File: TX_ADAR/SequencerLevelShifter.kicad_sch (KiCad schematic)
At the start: 12 parts, among them U15 TXB0101DBV, U16 TXB0101DBV, U17 TXB0101DBV, U18 TXB0101DBV

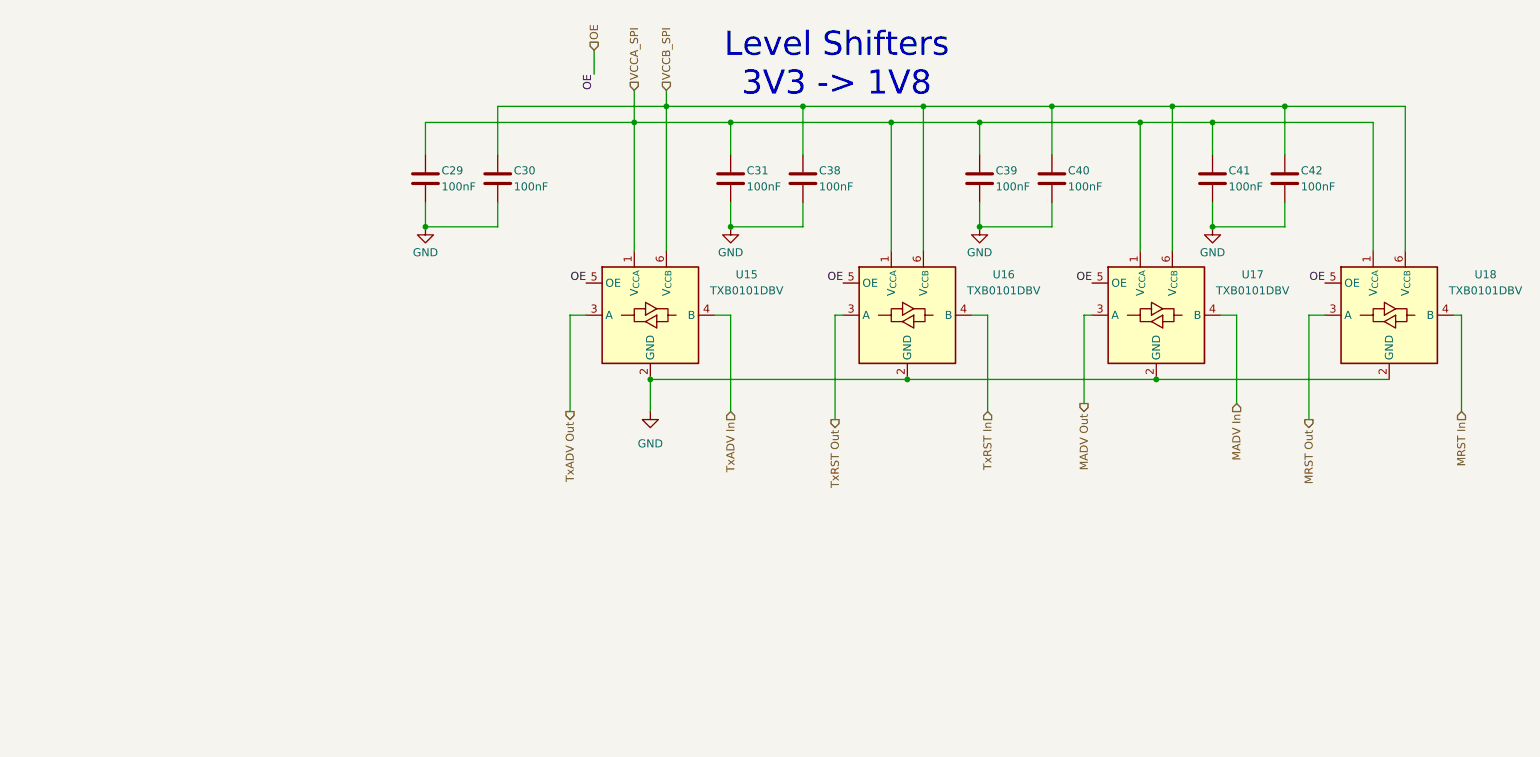
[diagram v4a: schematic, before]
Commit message: Added Level Shifters
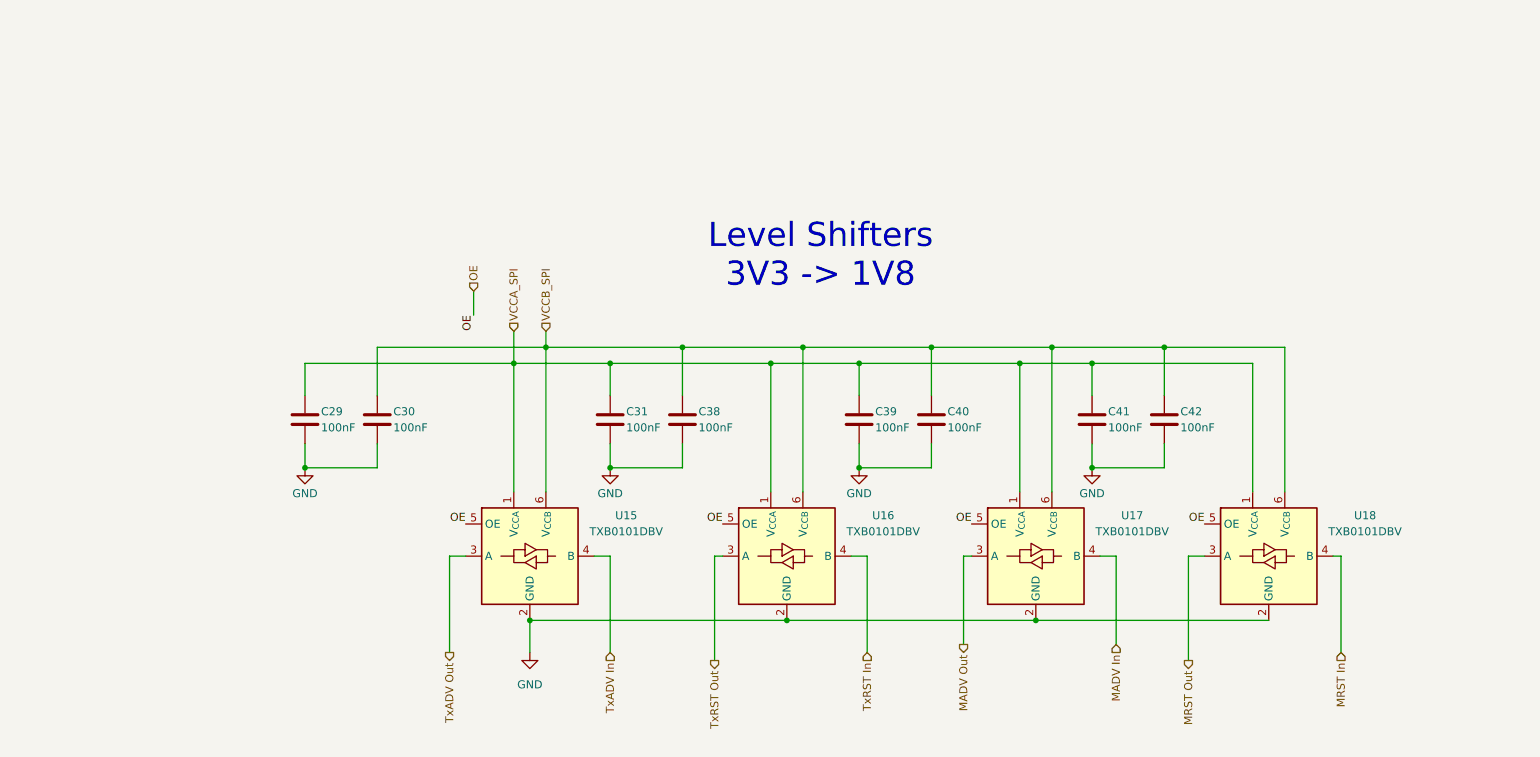
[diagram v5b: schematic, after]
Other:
- moved on the sheet: C29, C30, C31, C38, C39, C40, C41, C42, U15, U16, U17, U18

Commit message: Fixed tracks & added images to schem
NEED: Find 50 ohm impedance width for OSH Park
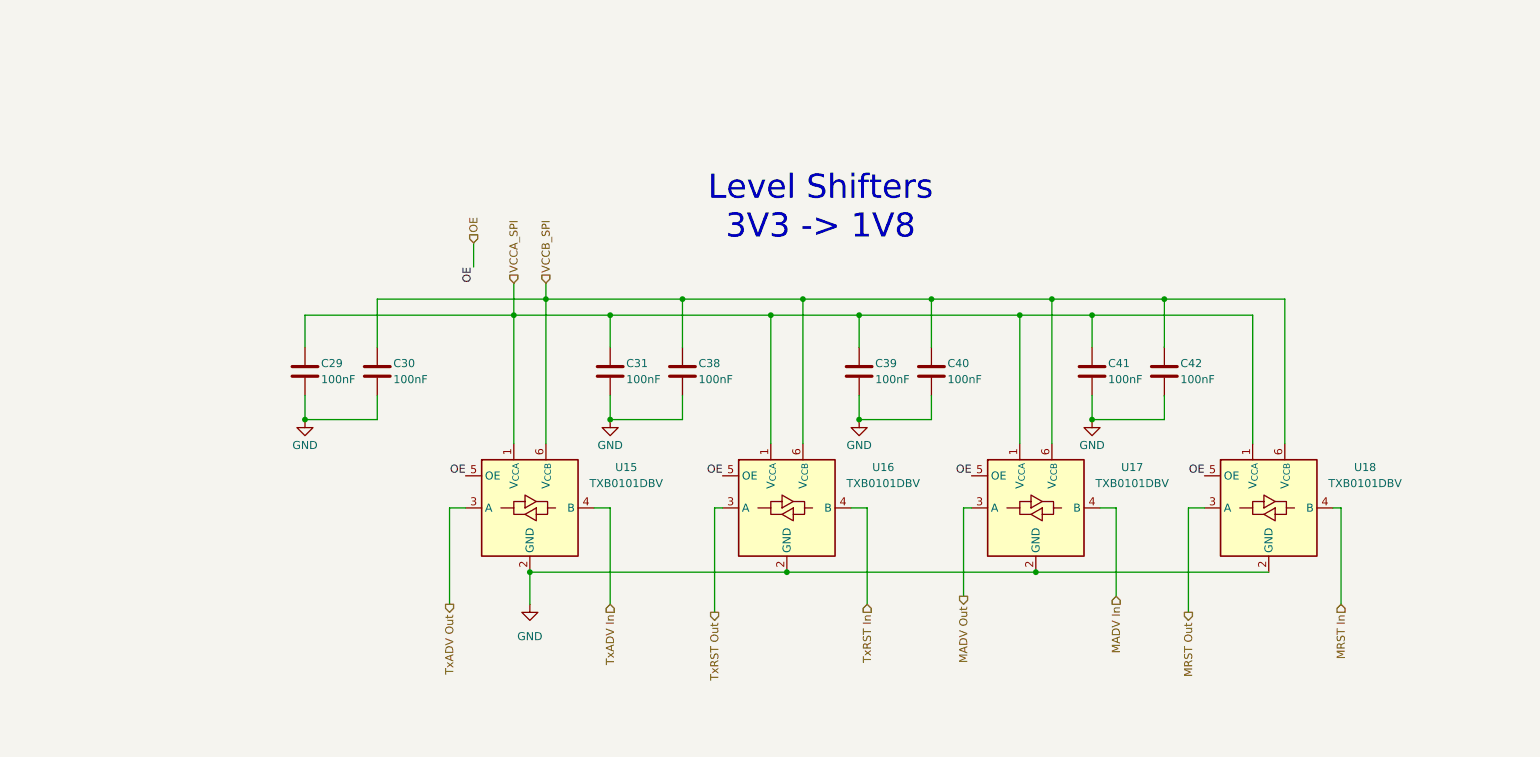
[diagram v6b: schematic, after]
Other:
- moved on the sheet: C29, C30, C31, C38, C39, C40, C41, C42, U15, U16, U17, U18
